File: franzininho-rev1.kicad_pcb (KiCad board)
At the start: 2 copper layers, 56.8 x 30 mm, 18 parts, among them J1 CONN_01X08, SW1 SW_RESET, U1 ATTINY85-20PU, U2 USB_conn

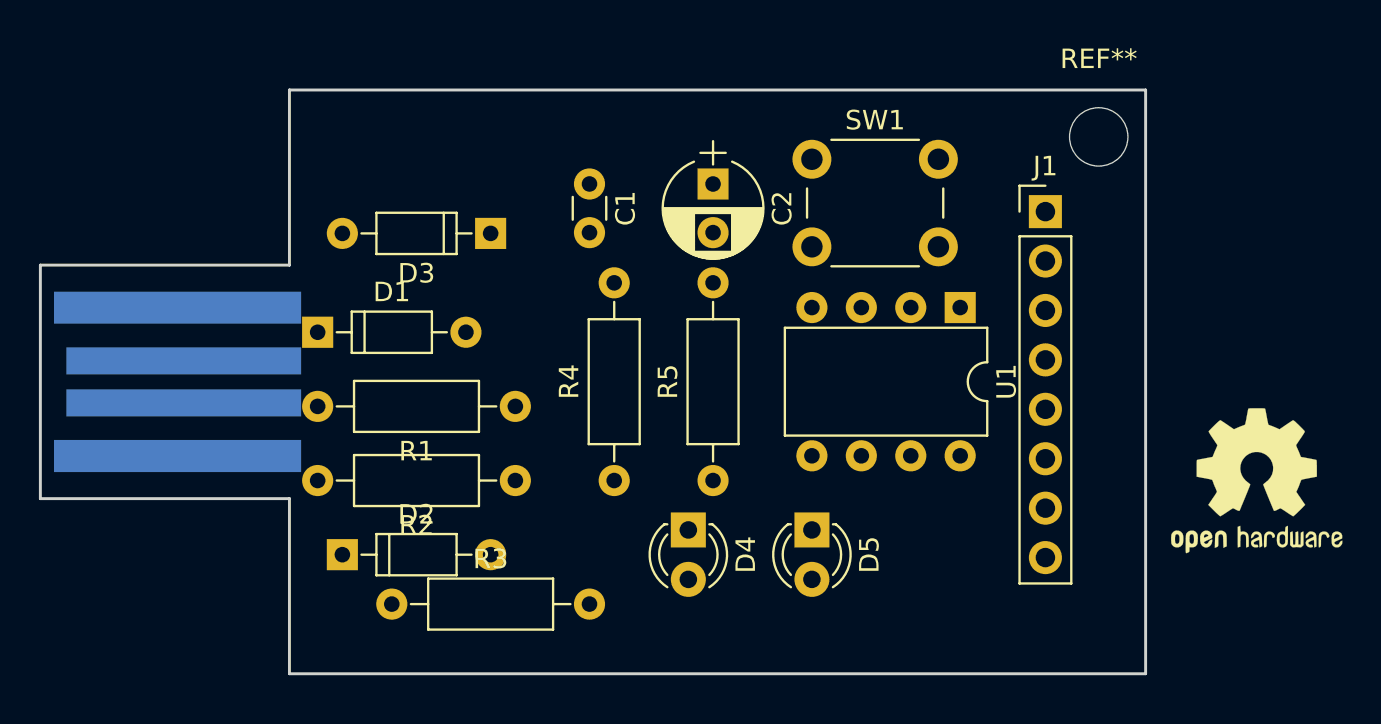
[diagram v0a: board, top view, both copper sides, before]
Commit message: add board layout
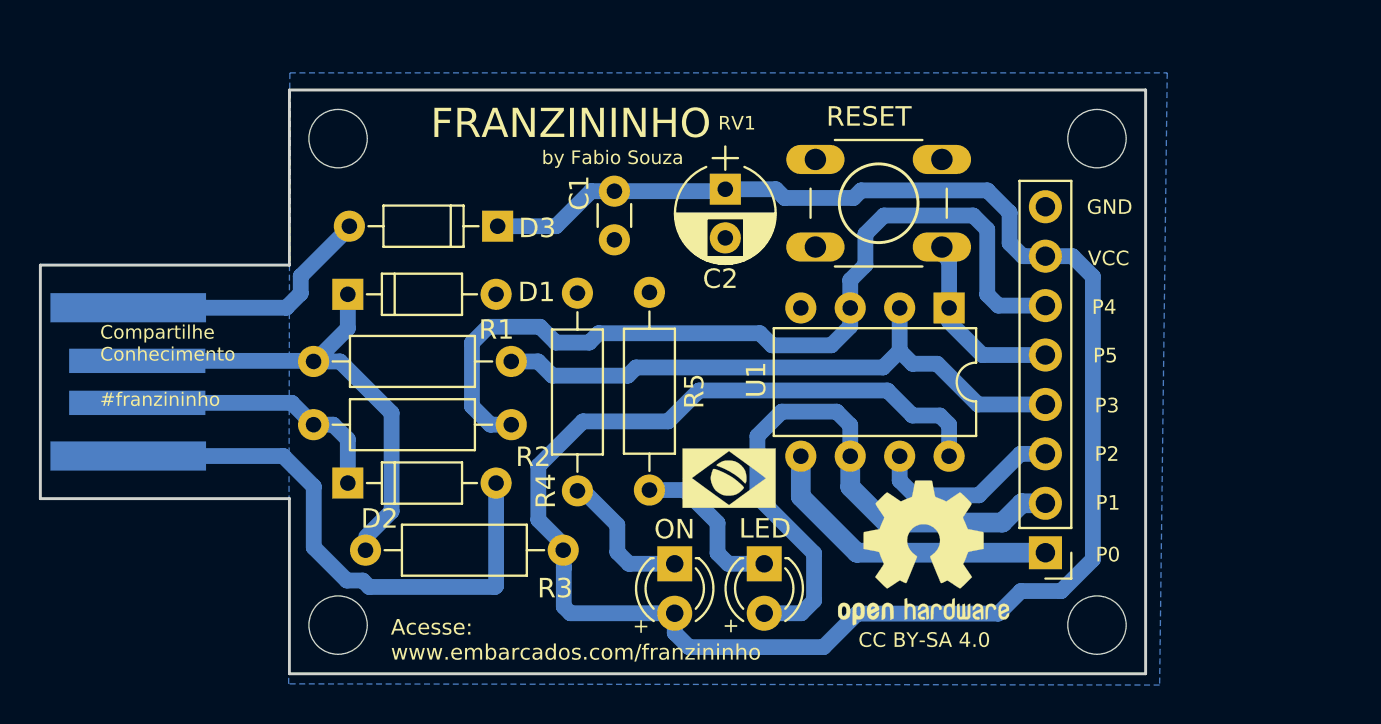
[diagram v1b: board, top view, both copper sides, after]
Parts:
- added G***: LOGO, logos:bandeira_brasil5x4, F.Cu at (167.2, 102.7)
- added REF**: MountingHole_3mm, Mounting_Holes:MountingHole_3mm, F.Cu at (147.1, 85.3)
- added REF**: MountingHole_3mm, Mounting_Holes:MountingHole_3mm, F.Cu at (147.1, 110.3)
- added REF**: MountingHole_3mm, Mounting_Holes:MountingHole_3mm, F.Cu at (186.1, 110.3)
- D4: value LED_ON -> ON
- SW1: value SW_RESET -> RESET; footprint Buttons_Switches_ThroughHole:SW_PUSH_6mm -> custom_6mm_push_btn
- U2: footprint usb_copper:USB_COPPER -> usb_copper:USB_COPPER_2
- moved J1 17.5 mm to (183.4, 106.6), turned to 180 degrees
- moved LOGO1 17.5 mm to (177.2, 106.6)
- moved R5 10.2 mm to (163.1, 93.2), turned to 270 degrees
- moved R3 9.24 mm to (158.7, 106.5), turned to 180 degrees
- moved SW1 8.06 mm to (178.1, 90.9), turned to 180 degrees
- moved D2 3.69 mm to (147.6, 103.0)
- moved D5 3.01 mm to (169.0, 107.2)
- moved R2 2.88 mm to (156.0, 100.0)
- moved D1 2.49 mm to (147.6, 93.3)
- moved R1 2.32 mm to (156.0, 96.8)
- moved R4 1.96 mm to (159.4, 103.4)
- moved D4 1.88 mm to (164.4, 107.2)
- moved C1 1.33 mm to (161.3, 88.0)
- moved C2 0.69 mm to (167.0, 87.9)
- moved U1 0.57 mm to (178.5, 94.0)
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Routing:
- net +5V: track 0.00 -> 112.4 mm
- net Net-(J1-Pad6): track 0.00 -> 45.2 mm
- net Net-(D5-Pad2): track 0.00 -> 33.2 mm
- net Net-(J1-Pad4): track 0.00 -> 31.6 mm
- net GND: track 0.00 -> 25.6 mm
- net Net-(D1-Pad1): track 0.00 -> 22.5 mm
- net Net-(J1-Pad1): track 0.00 -> 15.8 mm
- net Net-(D2-Pad1): track 0.00 -> 11.0 mm
- net Net-(D3-Pad2): track 0.00 -> 10.4 mm
- net Net-(J1-Pad3): track 0.00 -> 9.94 mm
- net Net-(J1-Pad5): track 0.00 -> 9.65 mm
- net Net-(D5-Pad1): track 0.00 -> 8.38 mm
- net Net-(D4-Pad1): track 0.00 -> 7.37 mm
- added copper zone on B.Cu, net GND
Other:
- board text added: "#franzininho"
- board text added: "+"
- board text added: "Acesse: www.embarcados.com/franzininho"
- board text added: "CC BY-SA 4.0"
- board text added: "Compartilhe Conhecimento"
- board text added: "FRANZININHO"
- board text added: "GND"
- board text added: "P0"
- board text added: "P1"
- board text added: "P2"
- board text added: "P3"
- board text added: "P4"
- board text added: "P5"
- board text added: "RV1"
- board text added: "VCC"
- board text added: "by Fabio Souza"
